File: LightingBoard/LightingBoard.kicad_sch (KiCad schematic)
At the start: 68 parts, among them J1 Barrel_Jack_Switch, J2 LED Out, J3 LED Out, J4 Programming, J5 UART, U1 AVR32DD20-E/REB, U10 AP2120N-5.0TRG1, U2 TL5580IDR, U3 INA180A2, U4 LMR33630ADDA, U5 MCP4725xxx-xCH, U6 INA180A2, U7 LMR33630ADDA, U8 MCP4725xxx-xCH, X1 XRCGB32M000F1S2KR0

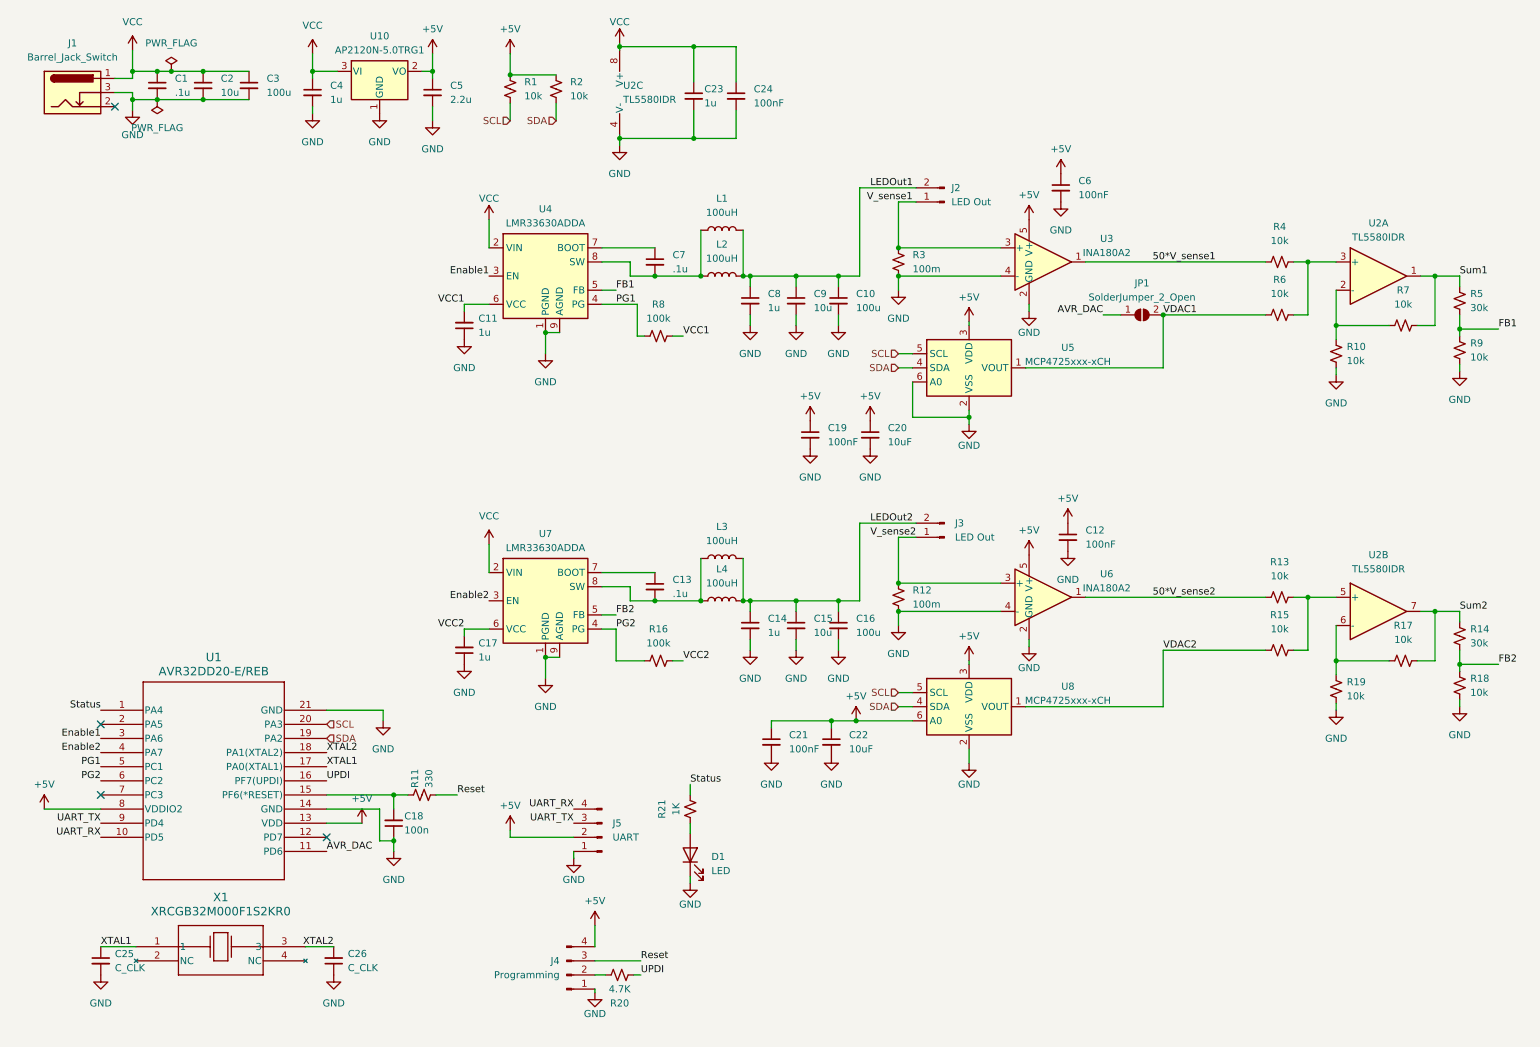
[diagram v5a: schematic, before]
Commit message: update to kicad 8
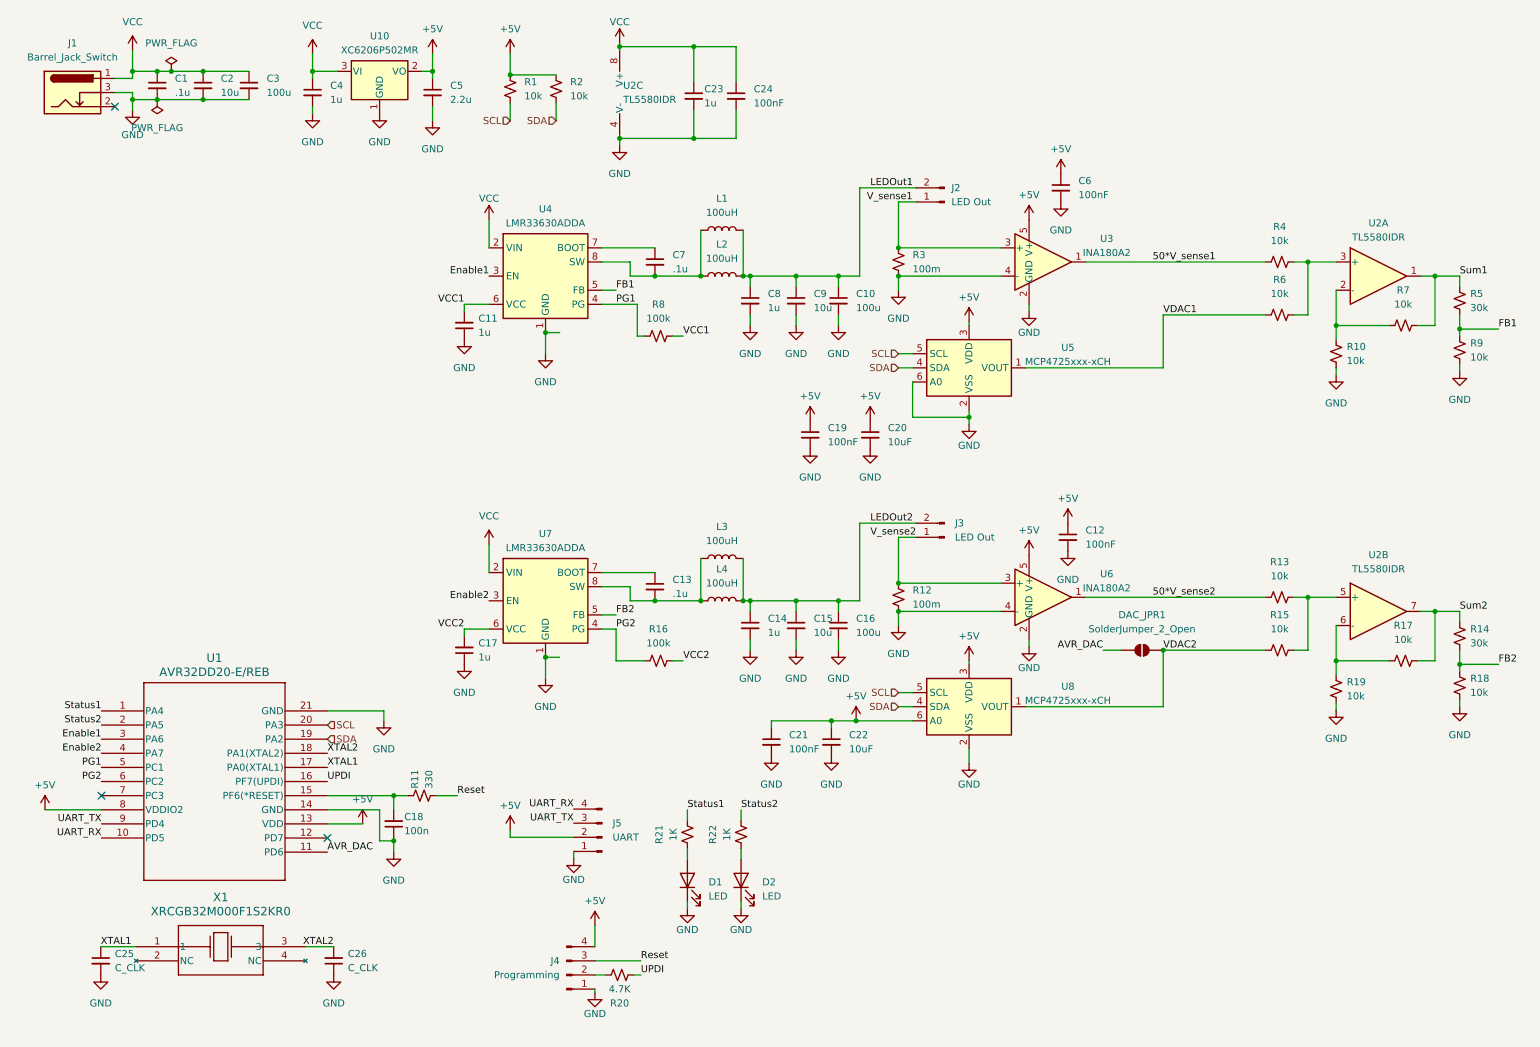
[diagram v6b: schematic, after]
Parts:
- added D2: LED, LED_SMD:LED_0805_2012Metric, symbol Device:LED
- added R22: 1K, Resistor_SMD:R_0603_1608Metric, symbol Device:R_Small_US
- U10: value AP2120N-5.0TRG1 -> XC6206P502MR
- renumbered JP1 to DAC_JPR1
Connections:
- net GND: now also D2.1 (K)
- net VDAC1: no longer DAC_JPR1.2 (B)
- net VDAC2: now also DAC_JPR1.2 (B)
- net Status2: now reaches U1.2 (PA5)
- net Status2: now also R22.2
- net Status renamed Status1
- new net: D2.2 (A), R22.1
- no-connect marks 4 -> 3
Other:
- moved on the sheet: D1, R21

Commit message: MORE PINS
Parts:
- removed C10, C16: 100u, Capacitor_SMD:CP_Elec_6.3x7.7, symbol Device:C_Small
- removed C11, C17, C23: 1u, Capacitor_SMD:C_0603_1608Metric, symbol Device:C_Small
- removed C14, C8: 1u, Capacitor_SMD:C_0805_2012Metric, symbol Device:C_Small
- removed C15, C9: 10u, Capacitor_SMD:C_0805_2012Metric, symbol Device:C_Small
- removed C18: 100n, Capacitor_SMD:C_0603_1608Metric, symbol Device:C_Small
- removed C21, C24, C6: 100nF, Capacitor_SMD:C_0603_1608Metric, symbol Device:C_Small
- removed C22: 10uF, Capacitor_SMD:C_0603_1608Metric, symbol Device:C_Small
- removed C7: .1u, Capacitor_SMD:C_0603_1608Metric, symbol Device:C_Small
- removed DAC_JPR1: SolderJumper_2_Open, Jumper:SolderJumper-2_P1.3mm_Open_RoundedPad1.0x1.5mm, symbol Jumper:SolderJumper_2_Open
- removed J2, J3: LED Out, Connector_PinSocket_2.54mm:PinSocket_1x02_P2.54mm_Vertical, symbol Connector:Conn_01x02_Pin
- removed L1, L3: 100uH, CustomFootprints:7447231101, symbol Device:L
- removed L2, L4: 100uH, CustomFootprints:IND_BOURNS_SDR1307, symbol Device:L
- removed R10, R13, R15, R17, R18, R19, R4, R6, R7, R9: 10k, Resistor_SMD:R_0603_1608Metric, symbol Device:R_Small_US
- removed R11: 330, Resistor_SMD:R_0603_1608Metric, symbol Device:R_Small_US
- removed R12, R3: 100m, Resistor_SMD:R_1206_3216Metric, symbol Device:R_Small_US
- removed R14, R5: 30k, Resistor_SMD:R_0603_1608Metric, symbol Device:R_Small_US
- removed R16, R8: 100k, Resistor_SMD:R_0603_1608Metric, symbol Device:R_Small_US
- removed U1: AVR32DD20-E/REB, Package_DFN_QFN:VQFN-20-1EP_3x3mm_P0.4mm_EP1.7x1.7mm, symbol CustomSymbols:AVR32DD20-E_REB
- removed U2: TL5580IDR, Package_SO:SOIC-8_3.9x4.9mm_P1.27mm, symbol Amplifier_Operational:LM358
- removed U3, U6: INA180A2, Package_TO_SOT_SMD:SOT-23-5, symbol Amplifier_Current:INA180A2
- removed U4, U7: LMR33630ADDA, Package_SO:Texas_HSOP-8-1EP_3.9x4.9mm_P1.27mm_ThermalVias, symbol Regulator_Switching:LMR33630ADDA
- removed U8: MCP4725xxx-xCH, Package_TO_SOT_SMD:SOT-23-6, symbol Analog_DAC:MCP4725xxx-xCH
- added J7: UART, Connector_JST:JST_SH_BM04B-SRSS-TB_1x04-1MP_P1.00mm_Vertical, symbol Connector:Conn_01x04_Pin
- added U1: AVR32DD28-I/STX, Package_DFN_QFN:VQFN-28-1EP_4x4mm_P0.45mm_EP2.4x2.4mm, symbol CustomSymbols:AVR32DD28-I_STX
- added U6: MCP4725xxx-xCH, Package_TO_SOT_SMD:SOT-23-6, symbol Analog_DAC:MCP4725xxx-xCH
- C1: value .1u -> 100n
- C13: value .1u -> 10uF
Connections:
- net +5V: now also C13.1, J7.2 (Pin_2), U1.18 (AVDD), U1.24 (VDD), U6.3 (VDD), U6.6 (A0)
- net AVR_DAC: now also U1.16 (PD6)
- net Enable1: now also U1.14 (PD4)
- net Enable2: now also U1.15 (PD5)
- net GND: now also C13.2, J7.1 (Pin_1), U1.19 (GND), U1.25 (GND), U1.29 (GND), U6.2 (VSS)
- net Reset: now also U1.22 (PF6(*RESET))
- net SCL: now also R2.2, U1.1 (PA3), U6.5 (SCL); no longer R1.2
- net SDA: now also R1.2, U1.28 (PA2), U6.4 (SDA); no longer R2.2
- net Status1: now also U1.11 (PD1)
- net Status2: now also U1.12 (PD2)
- net UART_RX: now also U1.7 (PC1)
- net UART_TX: now also U1.6 (PC0)
- net UPDI: now also U1.23 (PF7(UPDI))
- net XTAL1: now also U1.26 (PA0(XTALHF1))
- net XTAL2: now also U1.27 (PA1(XTALHF2))
- net VDAC1 renamed CC_Buck1/DAC_IN
- new net CC_Buck2/DAC_IN: U6.1 (VOUT)
- new net Enable0: U1.13 (PD3)
- new net UART_RX0: J7.4 (Pin_4), U1.3 (PA5)
- new net UART_TX0: J7.3 (Pin_3), U1.2 (PA4)
- no-connect marks 3 -> 9
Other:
- added sheet CC_Buck0 (CC_Buck.kicad_sch)
- added sheet CC_Buck1 (CC_Buck.kicad_sch)
- added sheet CC_Buck2 (CC_Buck.kicad_sch)
- moved on the sheet: C19, C20, C25, C26, U5, X1

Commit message: imma subsheet into your sheets
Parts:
- removed C19: 100nF, Capacitor_SMD:C_0603_1608Metric, symbol Device:C_Small
- removed C20: 10uF, Capacitor_SMD:C_0603_1608Metric, symbol Device:C_Small
- removed U1: AVR32DD28-I/STX, Package_DFN_QFN:VQFN-28-1EP_4x4mm_P0.45mm_EP2.4x2.4mm, symbol CustomSymbols:AVR32DD28-I_STX
- removed U5, U6: MCP4725xxx-xCH, Package_TO_SOT_SMD:SOT-23-6, symbol Analog_DAC:MCP4725xxx-xCH
- added C18: 100n, Capacitor_SMD:C_0603_1608Metric, symbol Device:C_Small
- added R11: 330, Resistor_SMD:R_0603_1608Metric, symbol Device:R_Small_US
- added R34: 100k, Resistor_SMD:R_0603_1608Metric, symbol Device:R_Small_US
- added TP1: TestPoint, TestPoint:TestPoint_Pad_D1.0mm, symbol Connector:TestPoint
- added U14: MCP4728, Package_SO:MSOP-10_3x3mm_P0.5mm, symbol Analog_DAC:MCP4728
- added U5: AVR32DD20-E/REB, Package_DFN_QFN:VQFN-20-1EP_3x3mm_P0.4mm_EP1.7x1.7mm, symbol CustomSymbols:AVR32DD20-E_REB
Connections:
- net +5V: now also R34.1, U14.1 (VDD), U5.13 (VDD), U5.8 (VDDIO2)
- net CC_Buck1/DAC_IN: now also U14.7 (VOUTB)
- net CC_Buck2/DAC_IN: now also U14.8 (VOUTC)
- net Enable0: now also U5.7 (PC3)
- net Enable1: now also U5.9 (PD4)
- net Enable2: now also U5.10 (PD5)
- net GND: now also C18.1, U14.10 (VSS), U14.4 (~{LDAC}), U5.14 (GND), U5.21 (GND)
- net Reset: now also R11.1
- net SCL: now also U14.2 (SCL), U5.20 (PA3)
- net SDA: now also U14.3 (SDA), U5.19 (PA2)
- net Status1: now also U5.5 (PC1)
- net Status2: now also U5.6 (PC2)
- net UART_RX: now also U5.12 (PD7)
- net UART_RX0: now also U5.2 (PA5)
- net UART_TX: now also U5.11 (PD6)
- net UART_TX0: now also U5.1 (PA4)
- net UPDI: now also U5.16 (PF7(UPDI))
- net XTAL1: now also U5.17 (PA0(XTAL1))
- net XTAL2: now also U5.18 (PA1(XTAL2))
- new net: C18.2, R11.2, U5.15 (PF6(*RESET))
- new net: TP1.1, U14.9 (VOUTD)
- new net: R34.2, U14.5 (RDY/~{BSY})
- new net CC_Buck0/DAC_IN: U14.6 (VOUTA)
- no-connect marks 9 -> 3
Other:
- moved on the sheet: C12, C13
